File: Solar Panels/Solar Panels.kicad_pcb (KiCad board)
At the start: 2 copper layers, 113 x 82.5 mm, 62 parts, among them J1 Conn_01x08_MountingPin, J2 Conn_01x08_MountingPin, J3 Conn_01x08_MountingPin, J4 Conn_01x02, J5 Conn_01x08_MountingPin

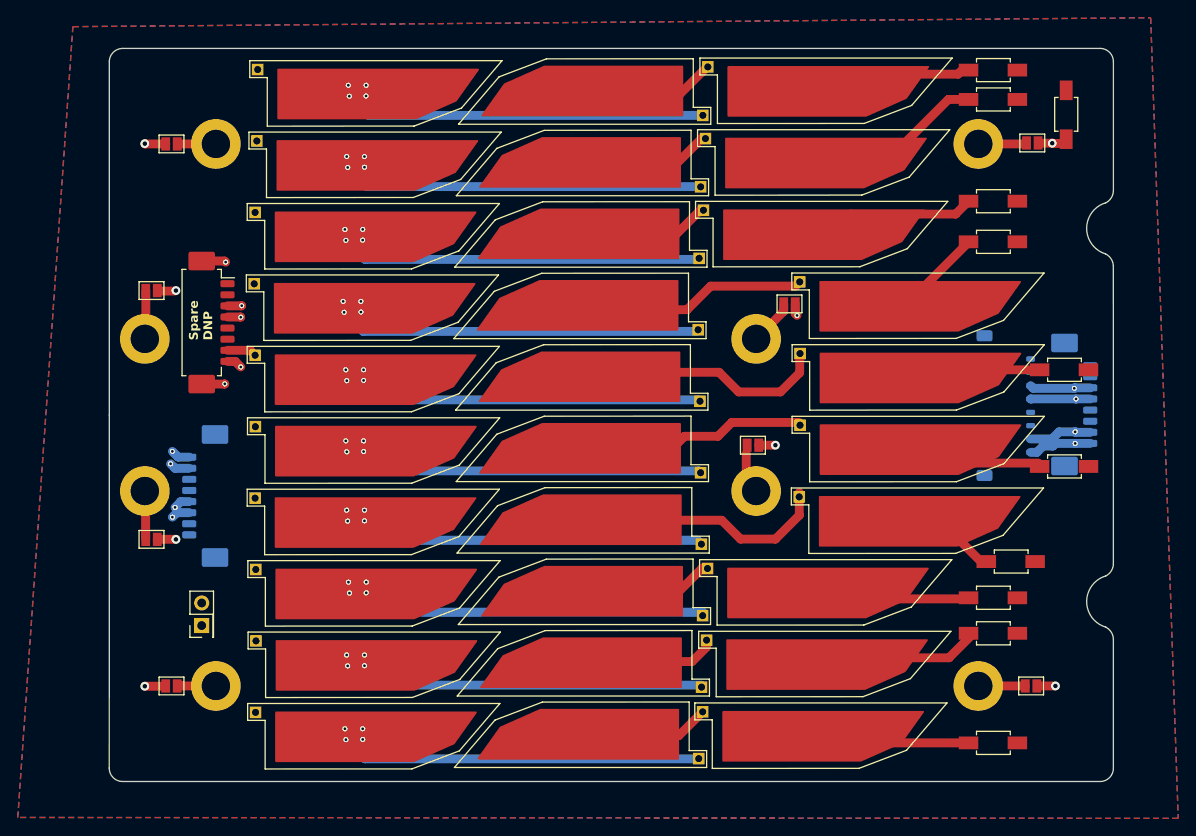
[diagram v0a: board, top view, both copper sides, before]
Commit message: Adjusted some placements and the footprint
Made some adjustments to the footprint (changing placement of the throughhole and the placement of solar cells)
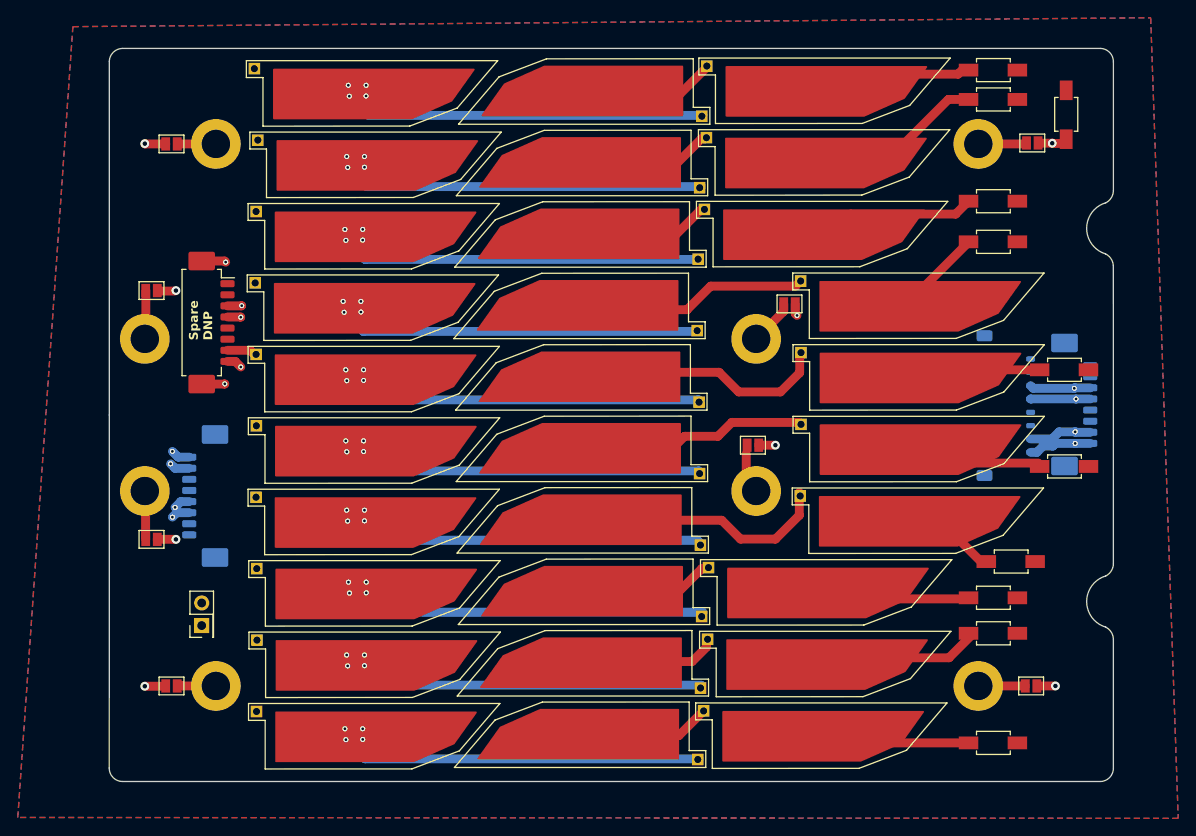
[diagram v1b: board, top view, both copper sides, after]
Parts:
- moved SC3 0.49 mm to (100.5, 79.6)
- moved SC1 0.22 mm to (151.4, 79.3)

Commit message: Made adjustments to Trisolx footprint and rerouted
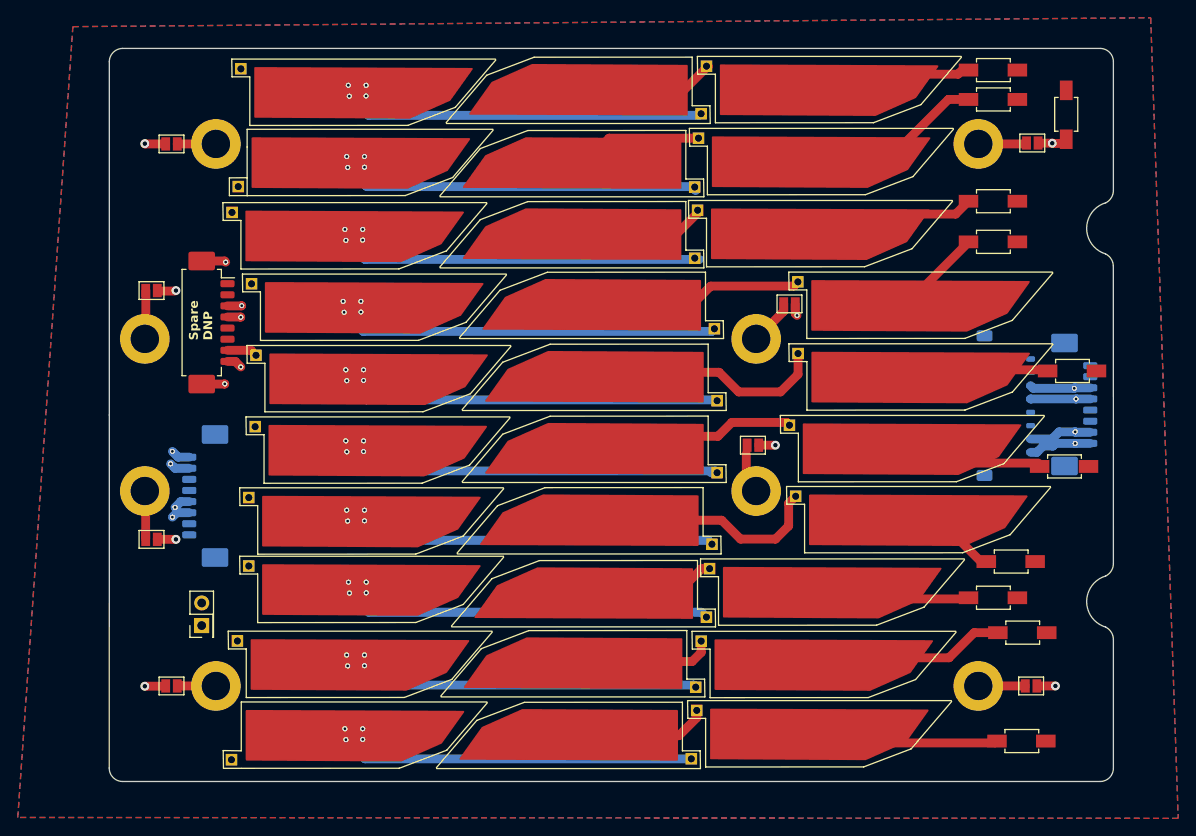
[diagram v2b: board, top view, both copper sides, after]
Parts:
- moved D9 3.30 mm to (177.8, 140.5)
- moved D10 3.21 mm to (177.7, 152.7)
- moved SC29 2.03 mm to (130.0, 152.2)
- moved SC5 1.86 mm to (130.4, 87.8)
- moved SC26 1.84 mm to (130.5, 144.1)
- moved SC8 1.68 mm to (130.4, 95.8)
- moved SC22 1.43 mm to (153.1, 135.8)
- moved SC30 1.42 mm to (99.3, 151.9)
- moved SC9 1.41 mm to (99.3, 95.7)
- moved SC2 1.40 mm to (131.1, 79.6)
- moved SC15 1.29 mm to (102.0, 111.8)
- moved SC1 1.27 mm to (152.7, 79.2)
- moved SC18 1.16 mm to (101.9, 119.8)
- moved SC10 0.99 mm to (163.0, 103.5)
- moved SC13 0.97 mm to (163.0, 111.6)
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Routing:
- net Net-(SC4--): track 4.90 -> 12.8 mm
- net Net-(SC28-+): track 10.9 -> 14.3 mm
- net Net-(SC25-+): track 19.3 -> 22.6 mm
- net Net-(SC17--): track 44.8 -> 47.3 mm
- net Net-(SC14--): track 44.7 -> 46.6 mm
- net Net-(SC11--): track 44.8 -> 46.7 mm
- net Net-(SC20--): track 44.9 -> 46.1 mm
- net Net-(SC16--): track 15.7 -> 14.8 mm
- net Net-(SC23--): track 44.7 -> 45.3 mm
- net Net-(SC19--): track 25.9 -> 25.3 mm
- net Net-(SC26--): track 44.7 -> 44.2 mm

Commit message: Adjust layout, add back-side cross-board pour
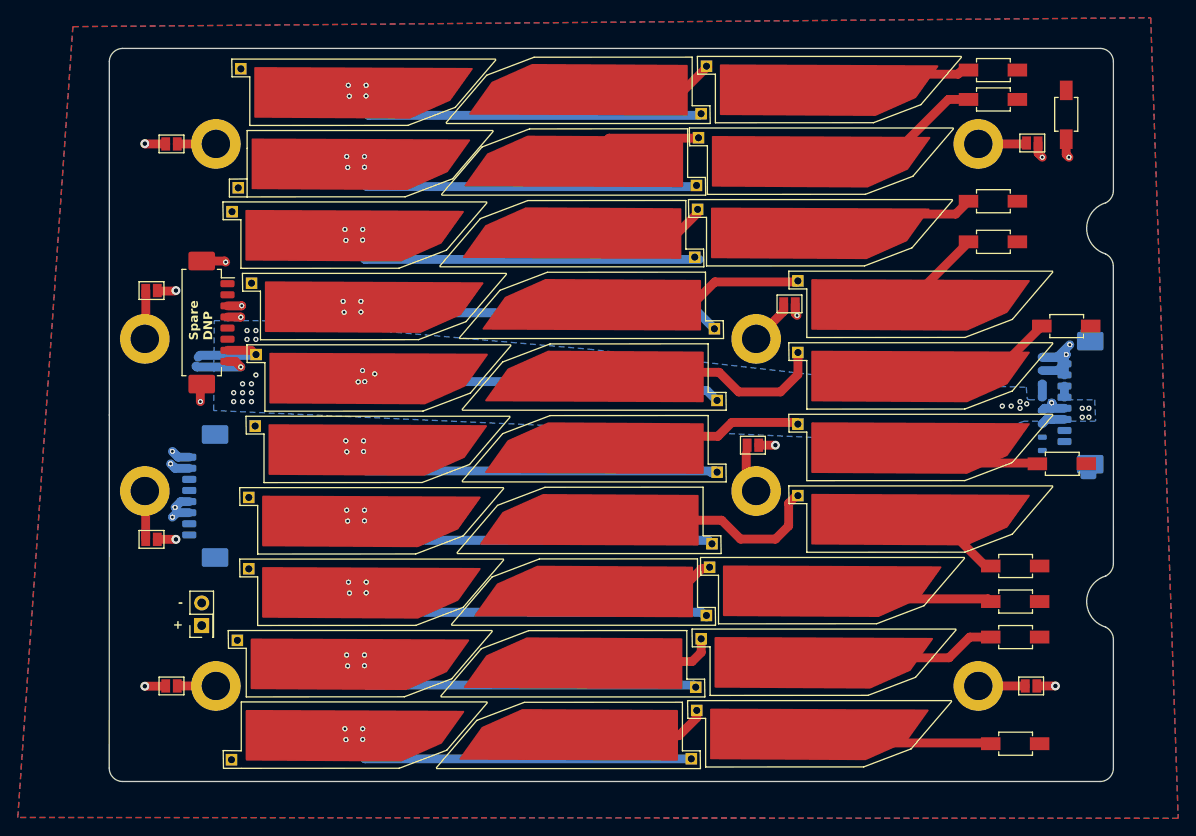
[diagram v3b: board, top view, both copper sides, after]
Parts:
- moved J5 6.90 mm to (182.8, 114.8), turned to -90 degrees
- moved D5 5.09 mm to (182.8, 106.0)
- moved D8 2.54 mm to (177.0, 137.0)
- moved J1 1.91 mm to (184.9, 114.6), turned to -90 degrees
- moved SC16 0.96 mm to (163.0, 119.5)
- moved D9 0.94 mm to (177.0, 141.0)
- moved D10 0.76 mm to (177.0, 153.0)
- moved D7 0.71 mm to (177.0, 133.0)
- moved D6 0.39 mm to (182.2, 121.5)
- moved SC24 0.32 mm to (101.2, 135.8)
- moved SC5 0.27 mm to (130.6, 87.7)
- moved SC19 0.26 mm to (163.0, 127.6)
- moved SC25 0.26 mm to (152.1, 143.7)
- moved SC23 0.18 mm to (131.7, 136.1)
- moved SC22 0.16 mm to (153.1, 135.6)
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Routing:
- net GND: track 29.7 -> 45.0 mm, vias 13 -> 14
- net +VDC: track 36.2 -> 26.1 mm, vias 8 -> 29
- net Net-(SC22-+): track 18.7 -> 21.2 mm
- net Net-(SC13-+): track 13.4 -> 15.7 mm
- net Net-(SC11--): track 46.7 -> 44.8 mm
- net Net-(SC14--): track 46.6 -> 45.4 mm
- net Net-(SC25-+): track 22.6 -> 21.6 mm
- net Net-(SC16--): track 14.8 -> 15.7 mm
- net Net-(SC28-+): track 14.3 -> 13.6 mm
- net Net-(SC19-+): track 12.5 -> 13.2 mm
- added copper zone on B.Cu, net +VDC
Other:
- board text added: "+"
- board text added: "-"
- board text added: "Pre-Order Checks: * Hide reference designators. * Check that current can flow across the board in the top layer pour. A blue-layer polygon helps add extra current-carrying capacity across the board. * DRC."
- board text added: "THIS SIDE IS NEGATIVE (orient toward MPI faceplate)"
- board text added: "THIS SIDE IS POSITIVE (orient away from MPI faceplate)"
- board text added: "This overlapping connector is intended to give the option between Microlock and Picoblade connectors."
- board text added: "pBlade|uLock"
- board text removed: "Pre-Order Checks: * Hide reference designators. * Check that current can flow across the board in the top layer pour."
